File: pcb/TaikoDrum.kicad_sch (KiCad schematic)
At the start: 34 parts, among them J1 USB_B_Micro, J2 Conn_02x04_Odd_Even, U1 STM32F103C8Tx, U3 LM358, U4 LM3940IMPX-3.3_NOPB, Y1 8Mhz

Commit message: Fixed all paths within the controller design. Swapped the micro USB footprint with JLCPCB compatible for auto assembly. Fixed clearance.
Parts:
- J1: footprint Connector_USB:USB_Mini-B_Wuerth_65100516121_Horizontal -> Library:MICRO-USB-SMD_5P-P0.65-H-F_C10418
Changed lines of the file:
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@@
 			)
 		)
-		(property "Footprint" "Connector_USB:USB_Mini-B_Wuerth_65100516121_Horizontal"
+		(property "Footprint" "Library:MICRO-USB-SMD_5P-P0.65-H-F_C10418"
 			(at 116.84 45.72 0)
 			(effects

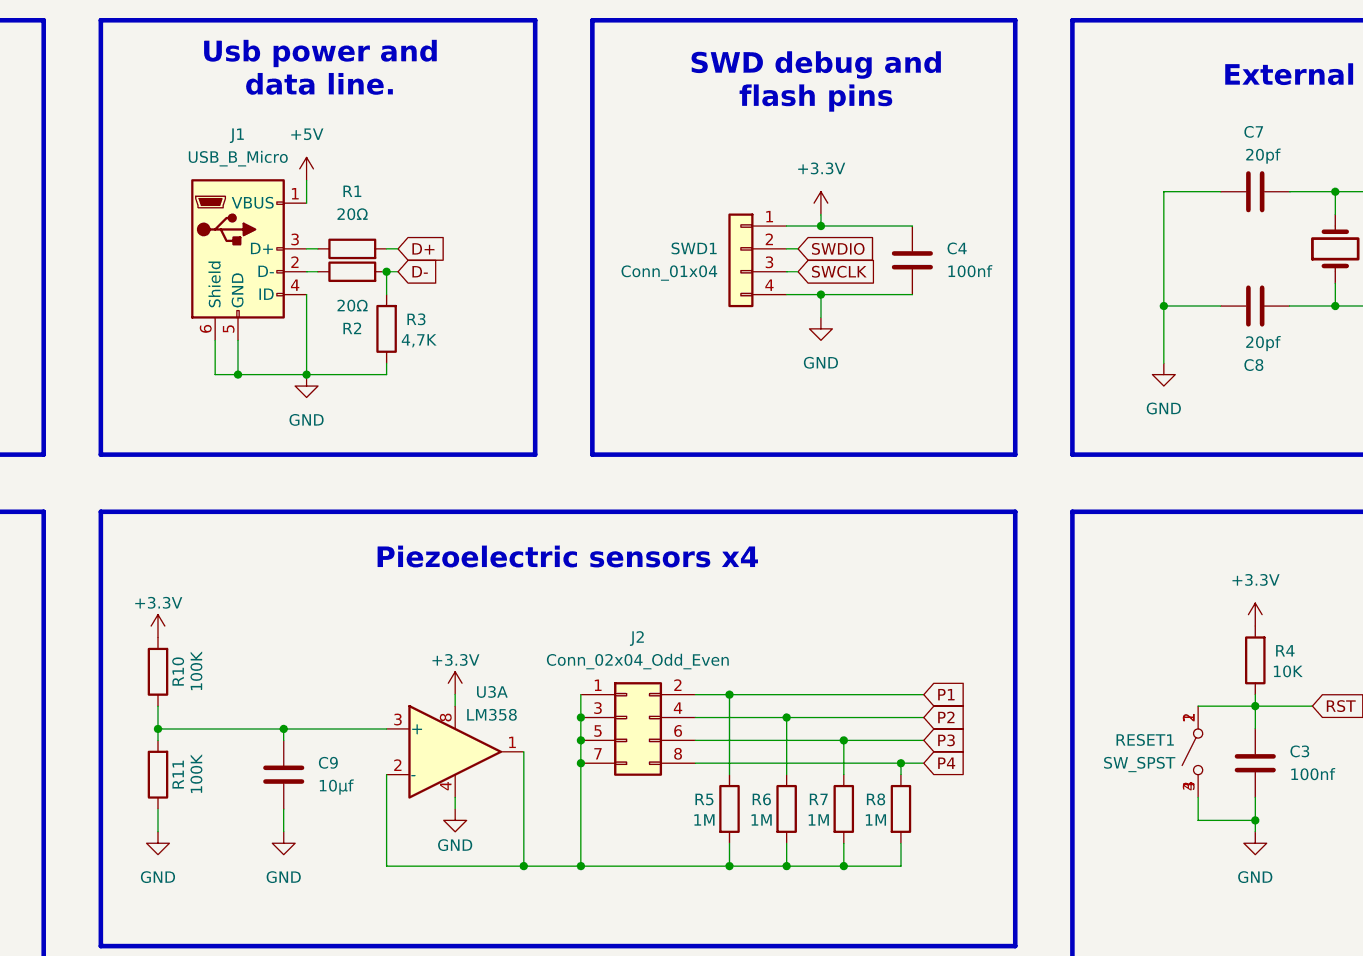
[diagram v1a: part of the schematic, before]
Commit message: Fixed the D+ line. the PCB schematic and layout is now 100% fully workable design. Fixed the button connection to be compatible with most generic tactile switches.
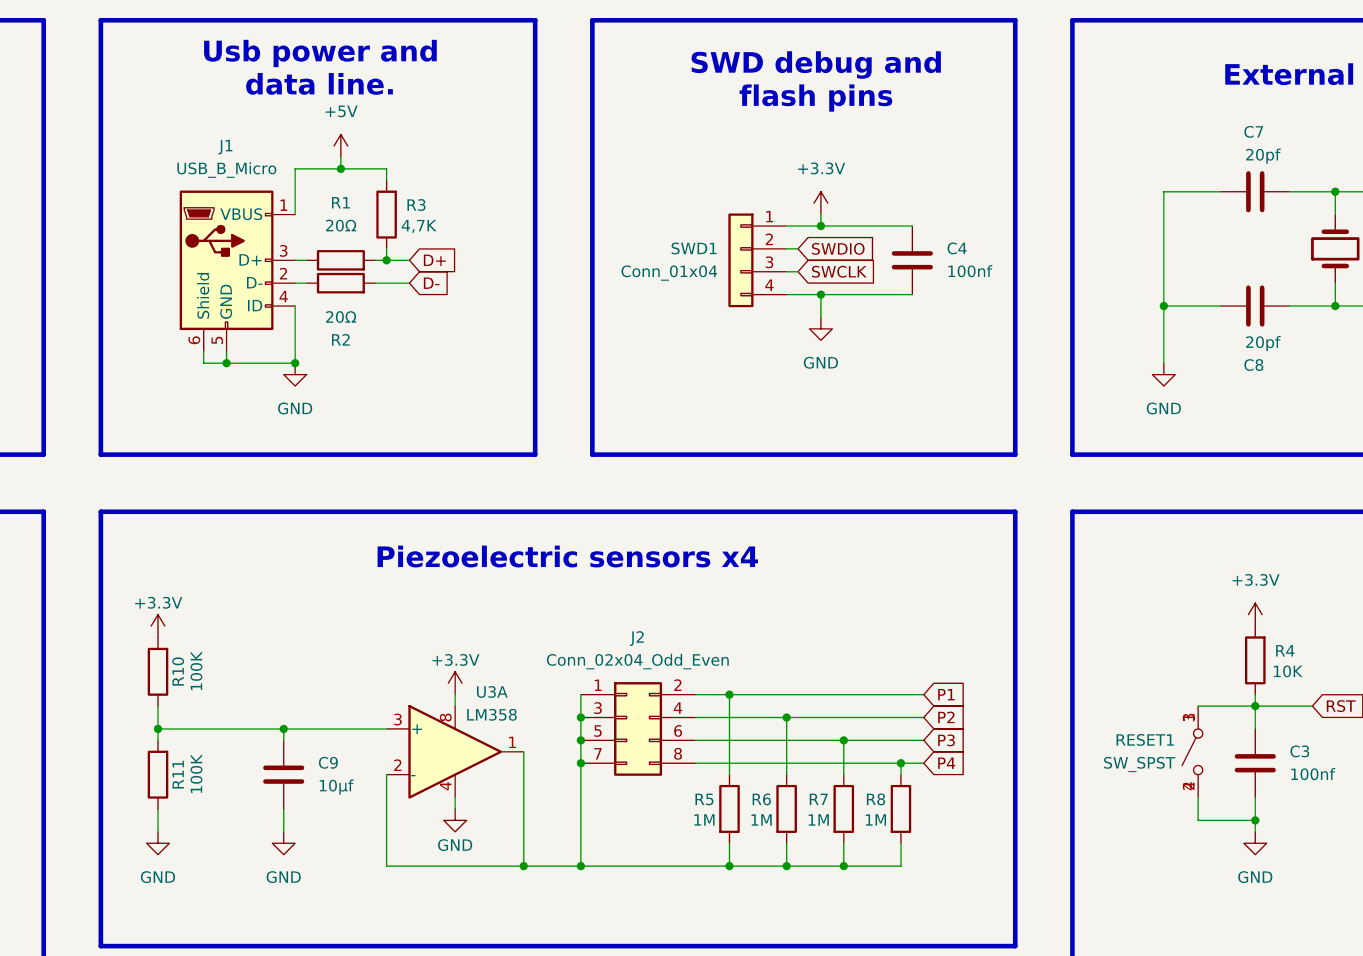
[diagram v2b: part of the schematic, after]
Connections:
- net +5V: now also R3.2
- net D+: now also R3.1
- net D-: no longer R3.2
- net GND: now also RESET1.2 (B); no longer R3.1, RESET1.3 (A)
- net RST: now also RESET1.3 (A); no longer RESET1.2 (B)
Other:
- moved on the sheet: J1, R1, R2, R3
